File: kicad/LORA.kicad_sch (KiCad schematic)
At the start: 0 parts

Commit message: [kicad] Added llcc68 lora-chip, [resources] Went over llcc68 datasheet + summarized essentials, added relevant documents
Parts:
- added U?: ~, symbol wireless_testboard:LLCC68
- added U?: ~, Package_DFN_QFN:QFN-24-1EP_4x4mm_P0.5mm_EP2.7x2.7mm, symbol wireless_testboard:LLCC68
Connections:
- new net GND: U?.2 (GND), U?.20 (GND), U?.25 (GND), U?.8 (GND)

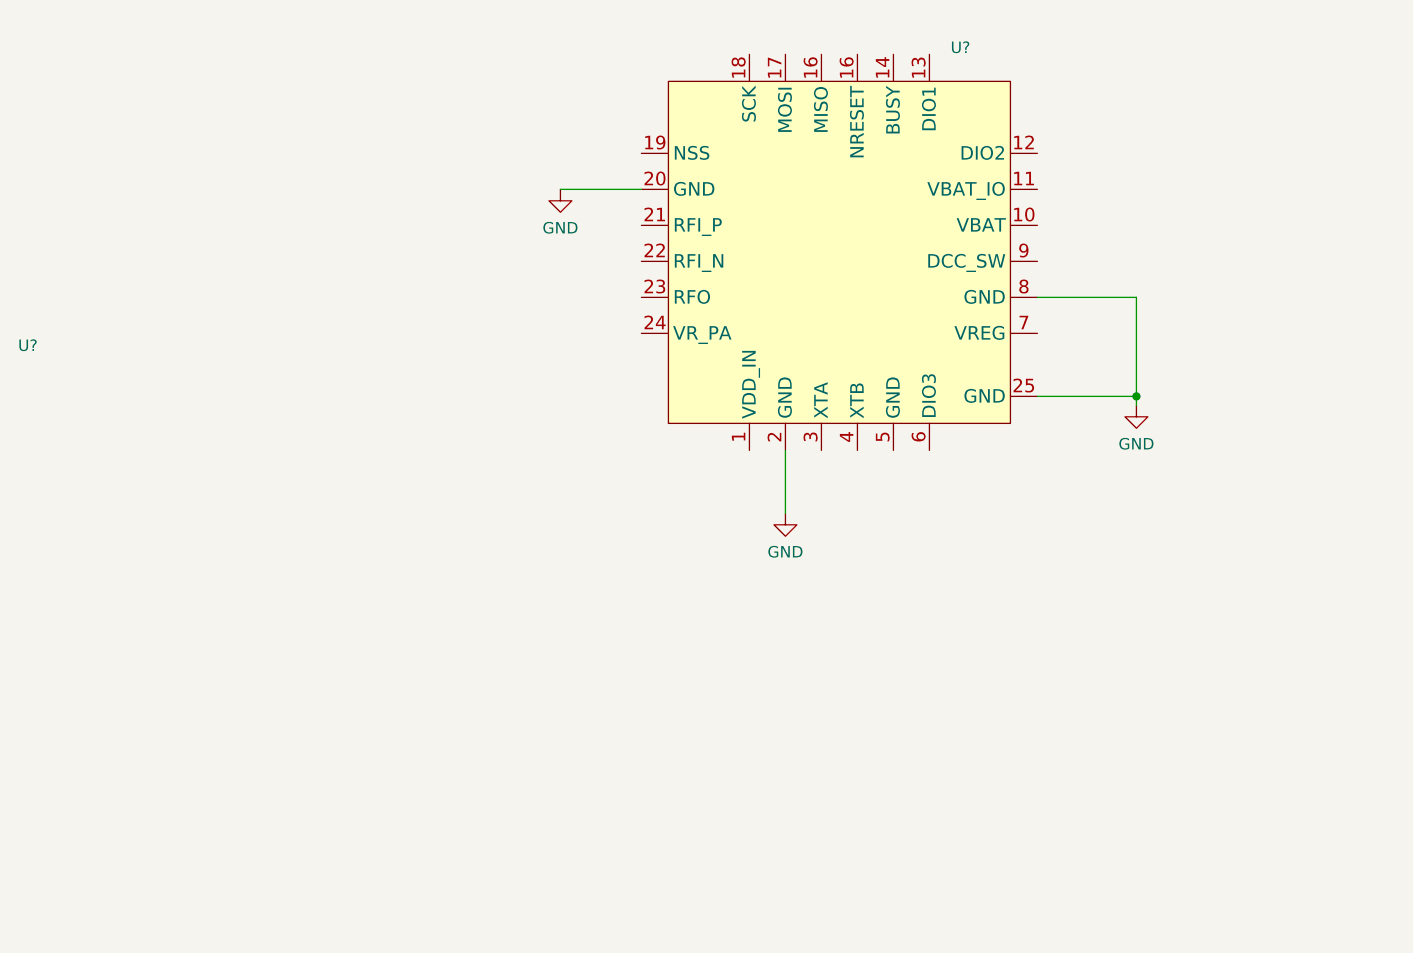
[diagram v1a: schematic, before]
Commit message: [kicad] fixed grid size, added oscillator |  to LoRa chip, added BLE and WiFi chip [resources] Added info relating to additions on kicad
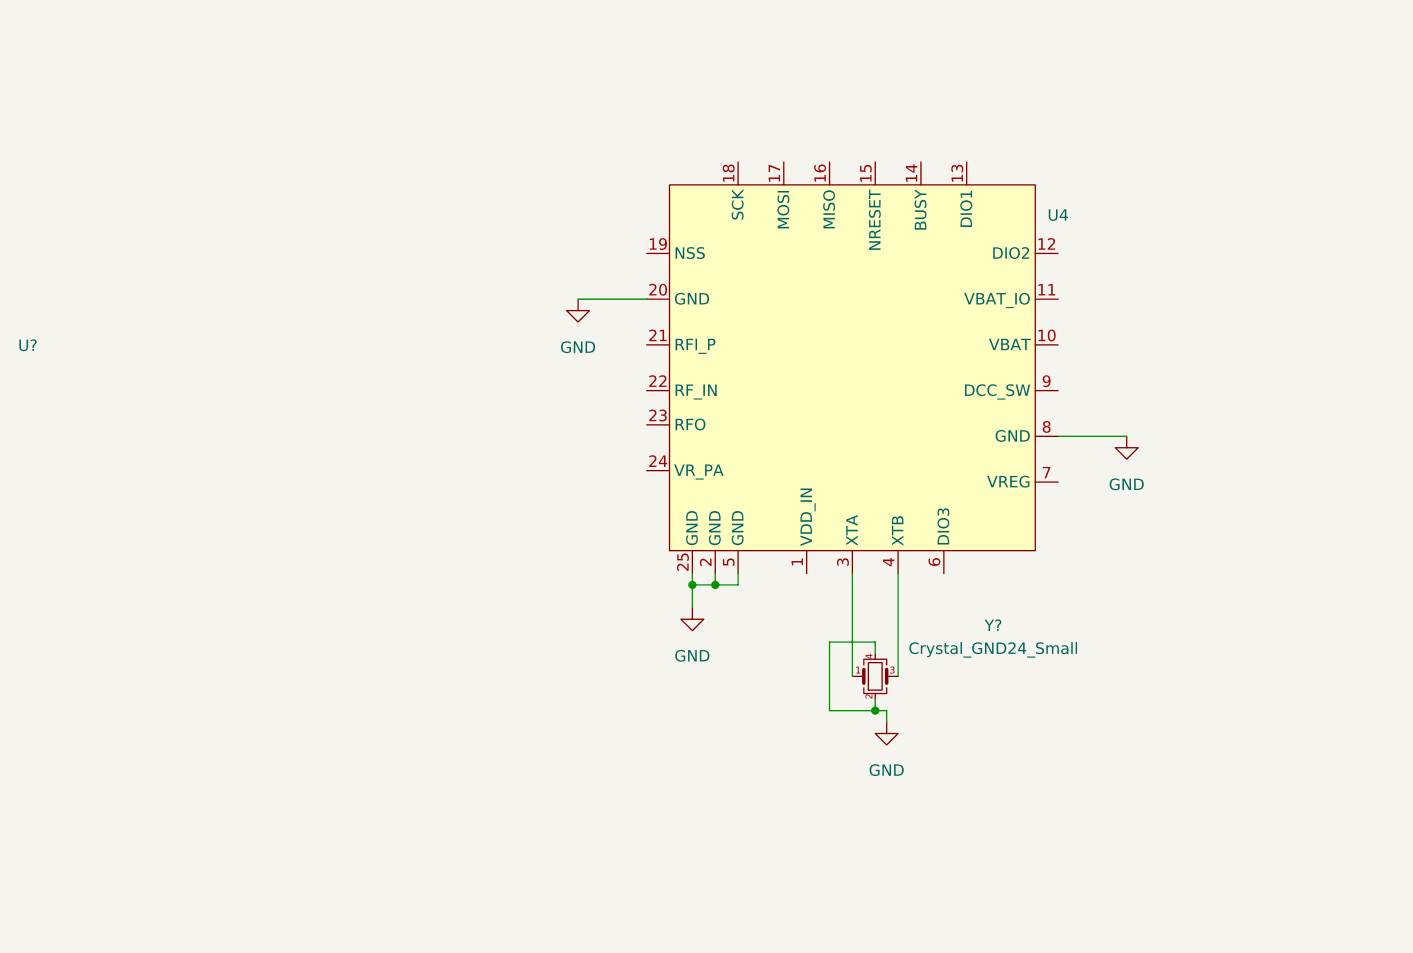
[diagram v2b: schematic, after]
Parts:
- removed U?: ~, Package_DFN_QFN:QFN-24-1EP_4x4mm_P0.5mm_EP2.7x2.7mm, symbol wireless_testboard:LLCC68
- added U4: ~, symbol hw_wireless_testboard:LLCC68
- added Y?: Crystal_GND24_Small, Crystal:Crystal_SMD_3225-4Pin_3.2x2.5mm_HandSoldering, symbol Device:Crystal_GND24_Small
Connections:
- net GND: now also U4.2 (GND), U4.20 (GND), U4.25 (GND), U4.5 (GND), U4.8 (GND), Y?.2, Y?.4
- new net: U4.3 (XTA), Y?.1
- new net: U4.4 (XTB), Y?.3

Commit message: fixed issues with footprints and symbols, minor connections drawn | TODO: DC-DC regulator empty footprint
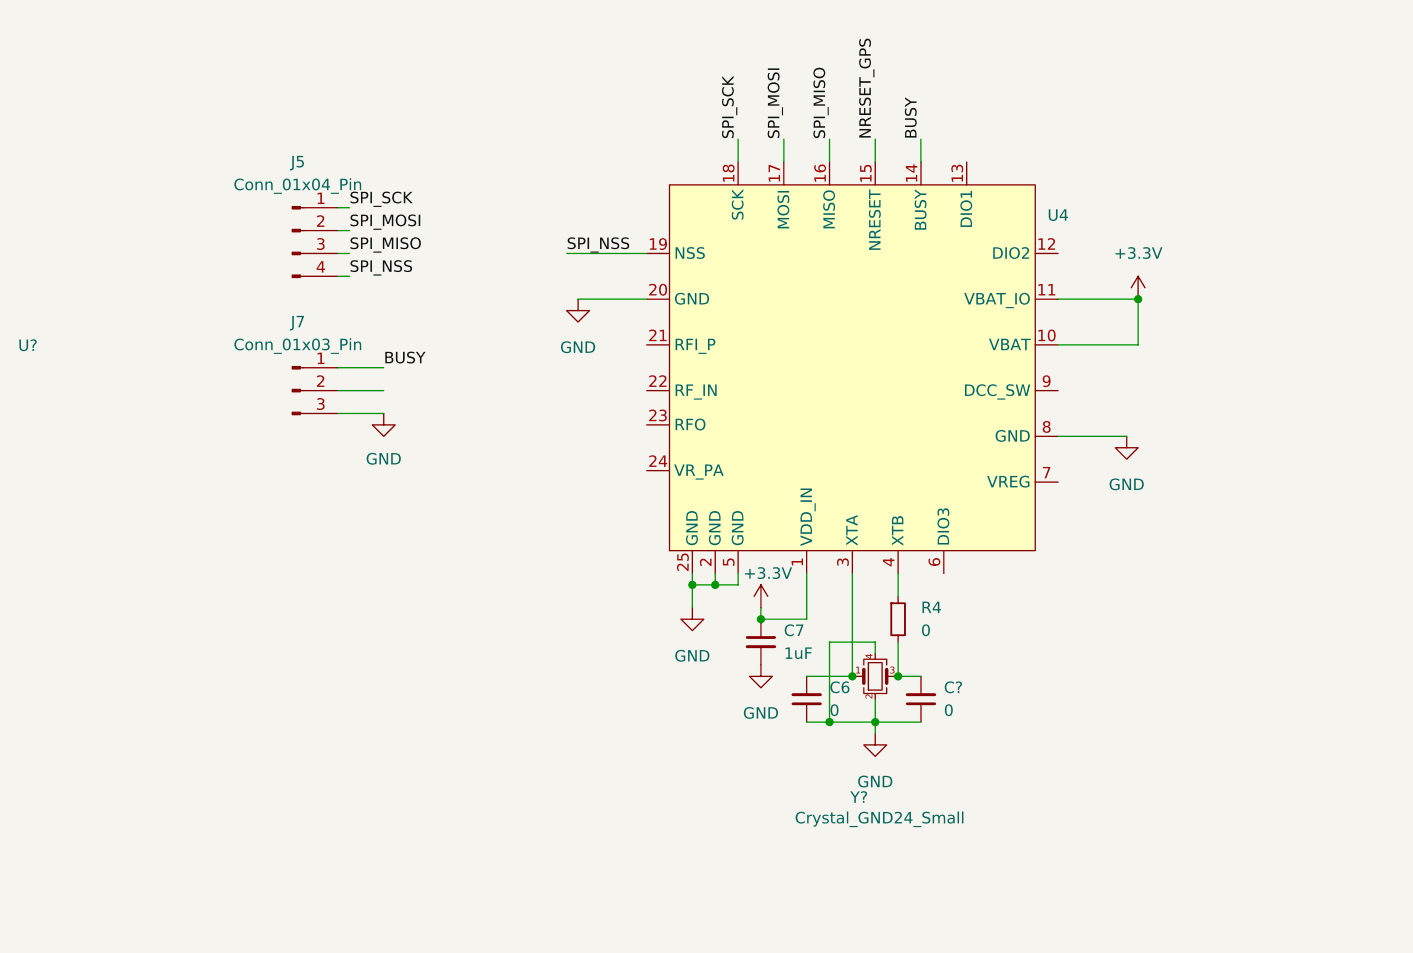
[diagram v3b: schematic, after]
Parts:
- added C6, C?: 0, symbol Device:C_Small
- added C7: 1uF, symbol Device:C_Small
- added J5: Conn_01x04_Pin, symbol Connector:Conn_01x04_Pin
- added J7: Conn_01x03_Pin, symbol Connector:Conn_01x03_Pin
- added R4: 0, Resistor_SMD:R_0402_1005Metric_Pad0.72x0.64mm_HandSolder, symbol Device:R_Small
- U4: footprint (none) -> Package_DFN_QFN:QFN-24-1EP_4x4mm_P0.5mm_EP2.7x2.7mm; MFR.Part (none) -> LLCC68IMLTRT; jlcpcb (none) -> C5120261
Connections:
- net GND: now also C6.1, C7.2, C?.1, J7.3 (Pin_3)
- net at U4.3 (XTA), Y?.1: now also C6.2
- net at U4.4 (XTB): now also R4.1; no longer Y?.3
- net +3.3V: now reaches U4.1 (VDD_IN)
- net +3.3V: now also U4.10 (VBAT), U4.11 (VBAT_IO), C7.1
- net BUSY: now reaches U4.14 (BUSY)
- net BUSY: now also J7.1 (Pin_1)
- net NRESET_GPS: now reaches U4.15 (NRESET)
- net SPI_MISO: now reaches U4.16 (MISO)
- net SPI_MISO: now also J5.3 (Pin_3)
- net SPI_MOSI: now reaches U4.17 (MOSI)
- net SPI_MOSI: now also J5.2 (Pin_2)
- net SPI_SCK: now reaches U4.18 (SCK)
- net SPI_SCK: now also J5.1 (Pin_1)
- net SPI_NSS: now reaches U4.19 (NSS)
- net SPI_NSS: now also J5.4 (Pin_4)
- new net: C?.2, R4.2, Y?.3

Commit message: finished bluetooth schematic apart from anteantenna-design, WiFi design started
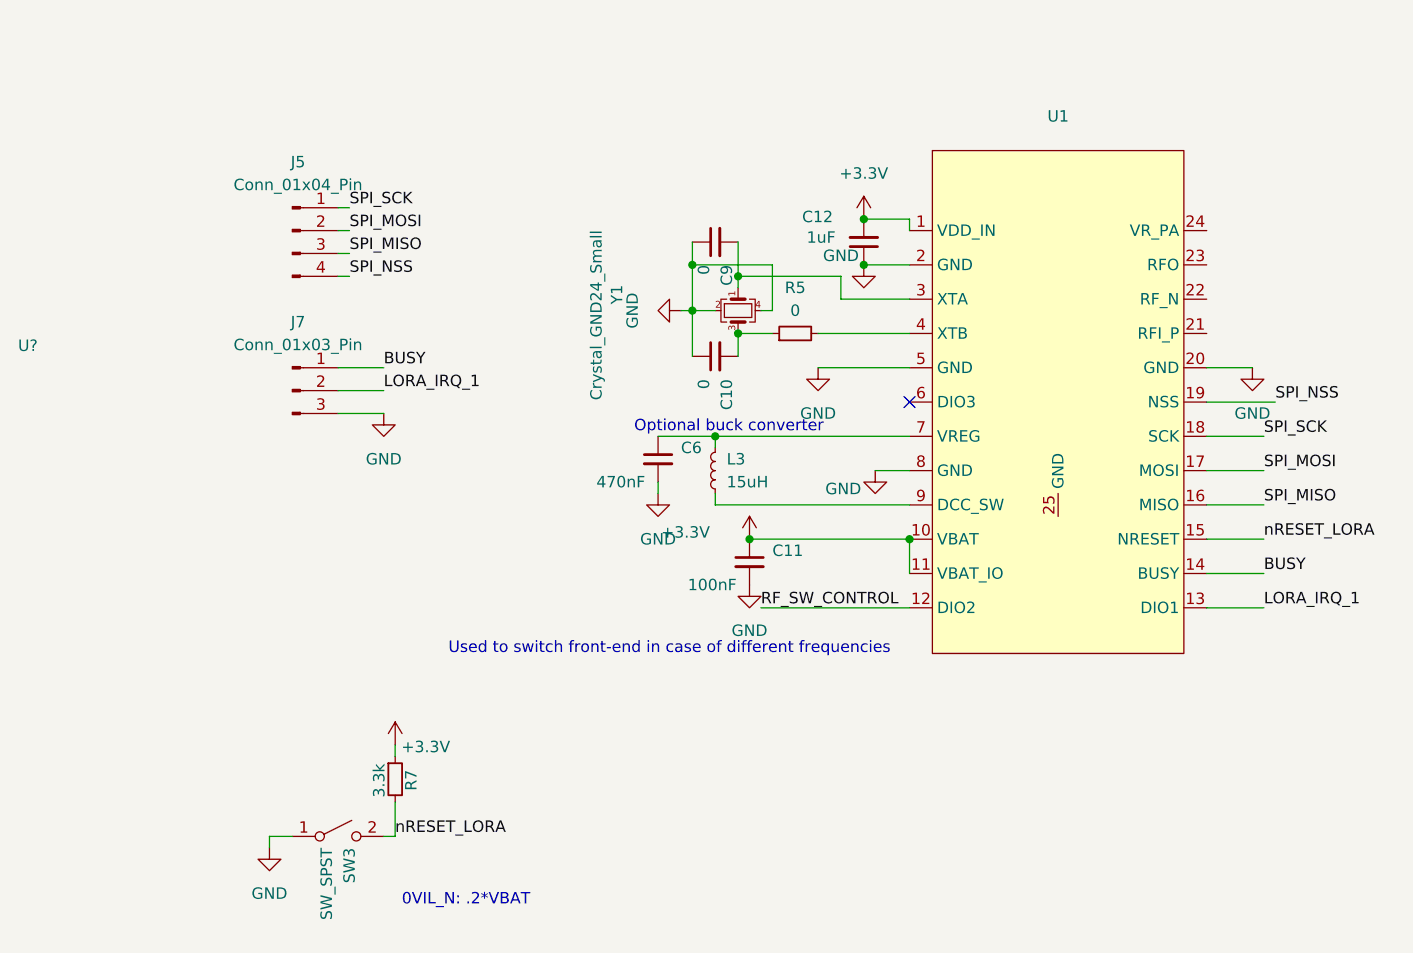
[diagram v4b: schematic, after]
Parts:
- removed C7: 1uF, symbol Device:C_Small
- removed C?: 0, symbol Device:C_Small
- removed R4: 0, Resistor_SMD:R_0402_1005Metric_Pad0.72x0.64mm_HandSolder, symbol Device:R_Small
- removed U4: ~, Package_DFN_QFN:QFN-24-1EP_4x4mm_P0.5mm_EP2.7x2.7mm, symbol hw_wireless_testboard:LLCC68
- removed Y?: Crystal_GND24_Small, Crystal:Crystal_SMD_3225-4Pin_3.2x2.5mm_HandSoldering, symbol Device:Crystal_GND24_Small
- added C10, C9: 0, symbol Device:C_Small
- added C11: 100nF, symbol Device:C_Small
- added C12: 1uF, symbol Device:C_Small
- added L3: 15uH, symbol Device:L_Small
- added R5: 0, Resistor_SMD:R_0402_1005Metric_Pad0.72x0.64mm_HandSolder, symbol Device:R_Small
- added R7: 3.3k, symbol Device:R_Small
- added SW3: SW_SPST, symbol Switch:SW_SPST
- added U1: ~, symbol hw_wireless_testboard:LLCC68
- added Y1: Crystal_GND24_Small, Crystal:Crystal_SMD_3225-4Pin_3.2x2.5mm_HandSoldering, symbol Device:Crystal_GND24_Small
- C6: value 0 -> 470nF
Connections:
- net +3.3V: now also C11.1, C12.2, R7.1, U1.1 (VDD_IN), U1.10 (VBAT), U1.11 (VBAT_IO)
- net BUSY: now also U1.14 (BUSY)
- net GND: now also C6.2, C10.1, C11.2, C12.1, C9.1, SW3.1 (A), U1.2 (GND), U1.20 (GND), U1.5 (GND), U1.8 (GND), Y1.2, Y1.4; no longer C6.1
- net SPI_MISO: now also U1.16 (MISO)
- net SPI_MOSI: now also U1.17 (MOSI)
- net SPI_NSS: now also U1.19 (NSS)
- net SPI_SCK: now also U1.18 (SCK)
- net LORA_IRQ_1: now reaches J7.2 (Pin_2)
- net LORA_IRQ_1: now also U1.13 (DIO1)
- new net: C6.1, L3.2, U1.7 (VREG)
- new net: C9.2, U1.3 (XTA), Y1.1
- new net: C10.2, R5.1, Y1.3
- new net: R5.2, U1.4 (XTB)
- new net: L3.1, U1.9 (DCC_SW)
- new net RF_SW_CONTROL: U1.12 (DIO2)
- new net nRESET_LORA: R7.2, SW3.2 (B), U1.15 (NRESET)
- no-connect marks 0 -> 1
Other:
- note added: "0VIL_N: .2*VBAT"
- note added: "Optional buck converter"
- note added: "Used to switch front-end in case of different frequencies"
